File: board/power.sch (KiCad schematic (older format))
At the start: 144 parts, among them P47 CONN_2, P48 CONN_2, SW1 SWITCH_INV, U14 TPS53319, U15 GBU15005-G, U16 TPS54560, U3 TPS54625, U4 TPS54625, U5 TPS54625, U6 TPS51200

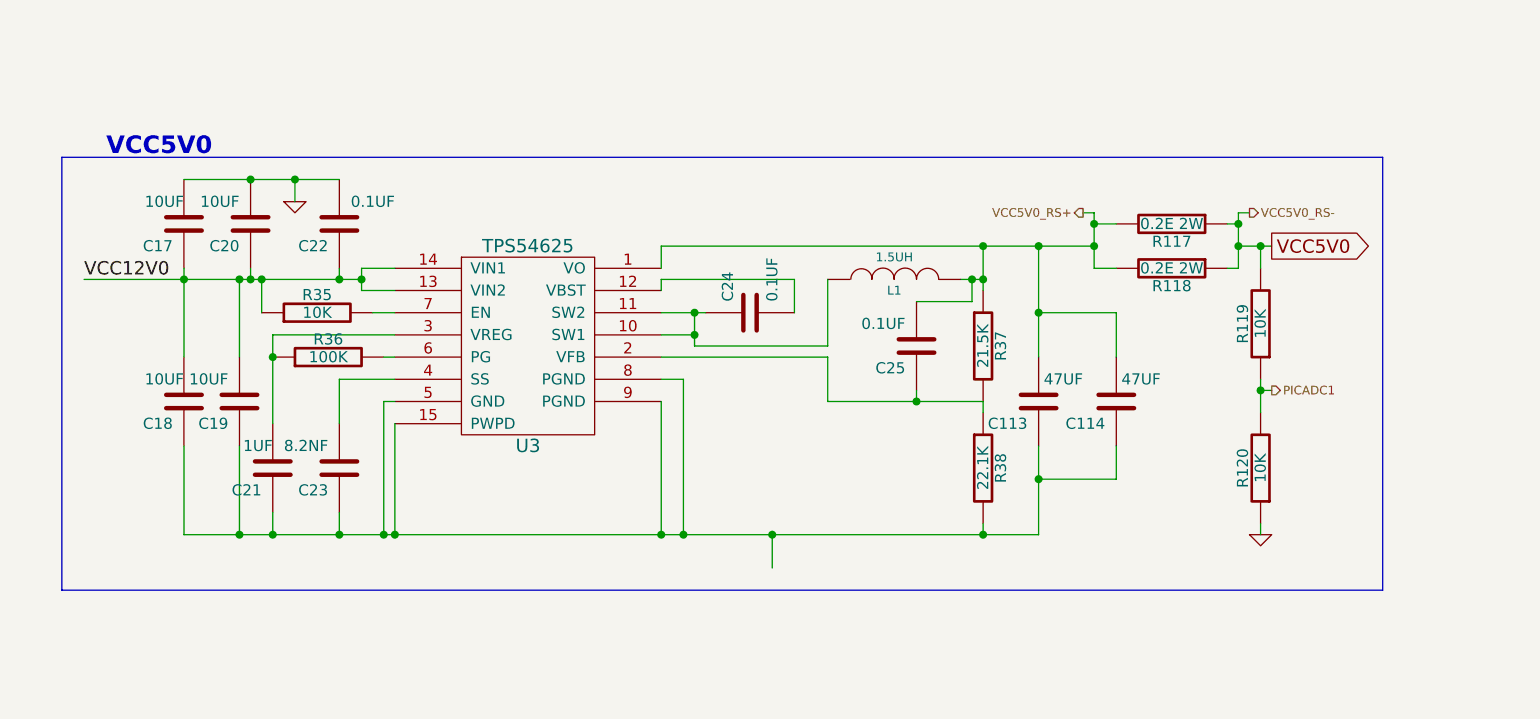
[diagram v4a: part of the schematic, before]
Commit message: Issue #934 - GTP routing
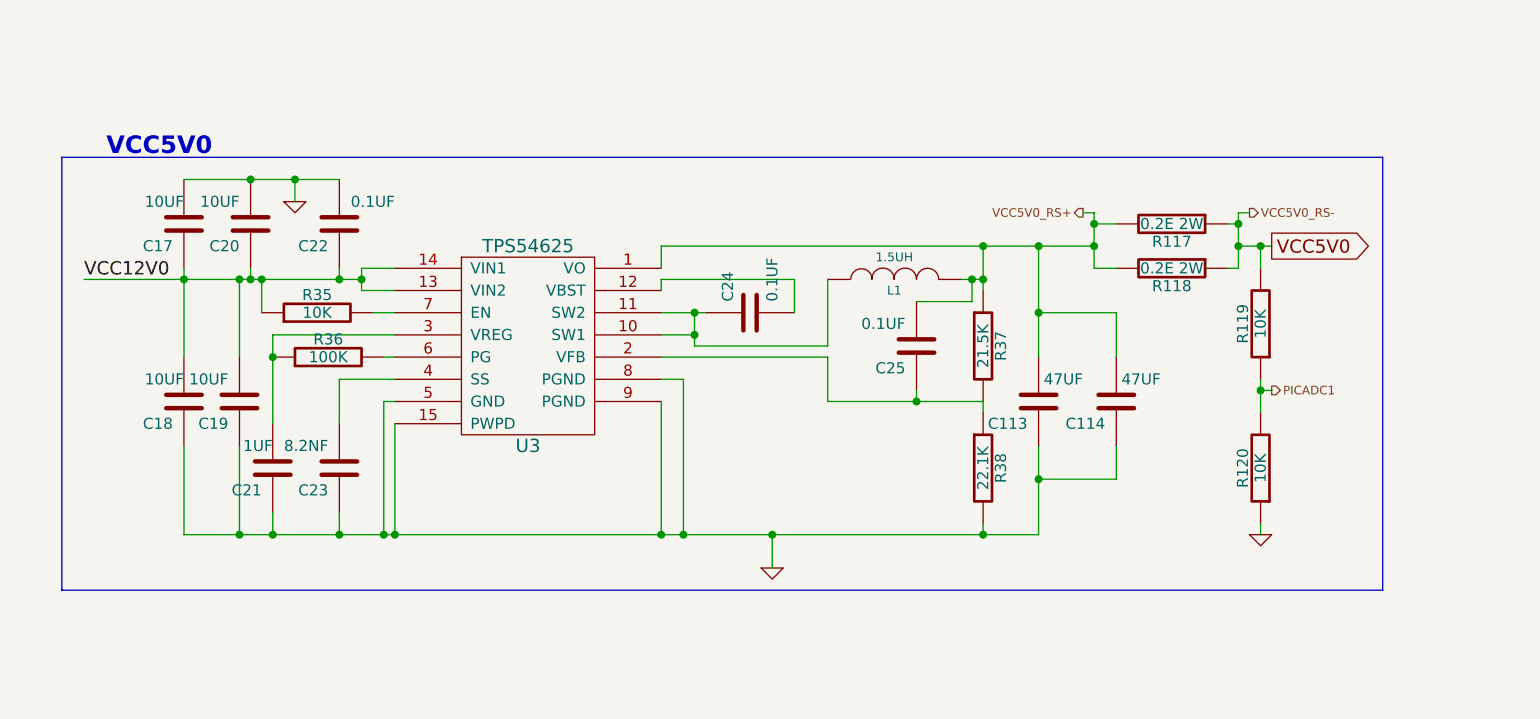
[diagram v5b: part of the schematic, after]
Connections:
- net GND: now also C113.1, C114.1, C18.1, C19.1, C21.1, C23.1, R38.2, U3.15 (PWPD), U3.5 (GND), U3.8 (PGND), U3.9 (PGND)
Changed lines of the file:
@@
 $Descr A3 16535 11693
 encoding utf-8
-Sheet 8 8
+Sheet 7 8
 Title "SP6N02"
-Date "27 feb 2014"
+Date "28 feb 2014"
 Rev "V1"
 Comp "Numato Lab"
@@
 $EndComp
 $Comp
-L GND #PWR12
+L GND #PWR03
 U 1 1 52DD9648
 P 11300 7700
-F 0 "#PWR12" H 11300 7700 30  0001 C CNN
+F 0 "#PWR03" H 11300 7700 30  0001 C CNN
 F 1 "GND" H 11300 7630 30  0001 C CNN
 F 2 "" H 11300 7700 60  0000 C CNN
@@
 $EndComp
 $Comp
-L GND #PWR16
+L GND #PWR04
 U 1 1 52DD9786
 P 12800 5350
-F 0 "#PWR16" H 12800 5350 30  0001 C CNN
+F 0 "#PWR04" H 12800 5350 30  0001 C CNN
 F 1 "GND" H 12800 5280 30  0001 C CNN
 F 2 "" H 12800 5350 60  0000 C CNN
@@
 $EndComp
 $Comp
-L GND #PWR15
+L GND #PWR05
 U 1 1 52DD9A04
 P 11500 1100
-F 0 "#PWR15" H 11500 1100 30  0001 C CNN
+F 0 "#PWR05" H 11500 1100 30  0001 C CNN
 F 1 "GND" H 11500 1030 30  0001 C CNN
 F 2 "" H 11500 1100 60  0000 C CNN
@@
 $EndComp
 $Comp
-L GND #PWR7
+L GND #PWR06
 U 1 1 52DD9A0A
 P 9400 2950
-F 0 "#PWR7" H 9400 2950 30  0001 C CNN
+F 0 "#PWR06" H 9400 2950 30  0001 C CNN
 F 1 "GND" H 9400 2880 30  0001 C CNN
 F 2 "" H 9400 2950 60  0000 C CNN
@@
 $EndComp
 $Comp
-L GND #PWR4
+L GND #PWR07
 U 1 1 52E1FEA6
 P 4000 1950
-F 0 "#PWR4" H 4000 1950 30  0001 C CNN
+F 0 "#PWR07" H 4000 1950 30  0001 C CNN
 F 1 "GND" H 4000 1880 30  0001 C CNN
 F 2 "" H 4000 1950 60  0000 C CNN
@@
 $EndComp
 $Comp
-L GND #PWR11
+L GND #PWR08
 U 1 1 52E4CA76
 P 10900 8600
-F 0 "#PWR11" H 10900 8600 30  0001 C CNN
+F 0 "#PWR08" H 10900 8600 30  0001 C CNN
 F 1 "GND" H 10900 8530 30  0001 C CNN
 F 2 "" H 10900 8600 60  0000 C CNN
@@
 $EndComp
 $Comp
-L GND #PWR8
+L GND #PWR09
 U 1 1 52E4CA88
 P 10450 9800
-F 0 "#PWR8" H 10450 9800 30  0001 C CNN
+F 0 "#PWR09" H 10450 9800 30  0001 C CNN
 F 1 "GND" H 10450 9730 30  0001 C CNN
 F 2 "" H 10450 9800 60  0000 C CNN
@@
 $EndComp
 $Comp
-L GND #PWR20
+L GND #PWR010
 U 1 1 52E4CAA0
 P 13800 9800
-F 0 "#PWR20" H 13800 9800 30  0001 C CNN
+F 0 "#PWR010" H 13800 9800 30  0001 C CNN
 F 1 "GND" H 13800 9730 30  0001 C CNN
 F 2 "" H 13800 9800 60  0000 C CNN
@@
 $EndComp
 $Comp
-L GND #PWR19
+L GND #PWR011
 U 1 1 52E4CAAC
 P 13200 9300
-F 0 "#PWR19" H 13200 9300 30  0001 C CNN
+F 0 "#PWR011" H 13200 9300 30  0001 C CNN
 F 1 "GND" H 13200 9230 30  0001 C CNN
 F 2 "" H 13200 9300 60  0000 C CNN
@@
 $EndComp
 $Comp
-L GND #PWR13
+L GND #PWR012
 U 1 1 52E4CAB8
 P 11350 9950
-F 0 "#PWR13" H 11350 9950 30  0001 C CNN
+F 0 "#PWR012" H 11350 9950 30  0001 C CNN
 F 1 "GND" H 11350 9880 30  0001 C CNN
 F 2 "" H 11350 9950 60  0000 C CNN
@@
 VCC3V3
 $Comp
-L GND #PWR17
+L GND #PWR013
 U 1 1 52E4CABF
 P 12800 9700
-F 0 "#PWR17" H 12800 9700 30  0001 C CNN
+F 0 "#PWR013" H 12800 9700 30  0001 C CNN
 F 1 "GND" H 12800 9630 30  0001 C CNN
 F 2 "" H 12800 9700 60  0000 C CNN
@@
 $EndComp
 $Comp
-L GND #PWR18
+L GND #PWR014
 U 1 1 52E4CACB
 P 13100 9950
-F 0 "#PWR18" H 13100 9950 30  0001 C CNN
+F 0 "#PWR014" H 13100 9950 30  0001 C CNN
 F 1 "GND" H 13100 9880 30  0001 C CNN
 F 2 "" H 13100 9950 60  0000 C CNN
@@
 $EndComp
 $Comp
-L GND #PWR9
+L GND #PWR015
 U 1 1 52F26CB0
 P 10650 3700
-F 0 "#PWR9" H 10650 3700 30  0001 C CNN
+F 0 "#PWR015" H 10650 3700 30  0001 C CNN
 F 1 "GND" H 10650 3630 30  0001 C CNN
 F 2 "" H 10650 3700 60  0000 C CNN
@@
 $EndComp
 $Comp
-L GND #PWR10
+L GND #PWR016
 U 1 1 52F2BB58
 P 10900 6200
-F 0 "#PWR10" H 10900 6200 30  0001 C CNN
+F 0 "#PWR016" H 10900 6200 30  0001 C CNN
 F 1 "GND" H 10900 6130 30  0001 C CNN
 F 2 "" H 10900 6200 60  0000 C CNN
@@
 $EndComp
 $Comp
-L GND #PWR14
+L GND #PWR017
 U 1 1 52F2C00C
 P 11450 6150
-F 0 "#PWR14" H 11450 6150 30  0001 C CNN
+F 0 "#PWR017" H 11450 6150 30  0001 C CNN
 F 1 "GND" H 11450 6080 30  0001 C CNN
 F 2 "" H 11450 6150 60  0000 C CNN
@@
 $EndComp
 $Comp
-L GND #PWR5
+L GND #PWR018
 U 1 1 52FA3E62
 P 6250 9400
-F 0 "#PWR5" H 6250 9400 30  0001 C CNN
+F 0 "#PWR018" H 6250 9400 30  0001 C CNN
 F 1 "GND" H 6250 9330 30  0001 C CNN
 F 2 "" H 6250 9400 60  0000 C CNN
@@
 $EndComp
 $Comp
-L GND #PWR3
+L GND #PWR019
 U 1 1 52FA3EB9
 P 1900 7900
-F 0 "#PWR3" H 1900 7900 30  0001 C CNN
+F 0 "#PWR019" H 1900 7900 30  0001 C CNN
 F 1 "GND" H 1900 7830 30  0001 C CNN
 F 2 "" H 1900 7900 60  0000 C CNN
@@
 	850  7700 6800 7700
 Wire Bus Line
-	6800 9650 6800 7700
+	6800 7700 6800 9650
 Wire Bus Line
-	850  9650 6800 9650
+	6800 9650 850  9650
 Connection ~ 4150 1250
 Wire Wire Line
@@
 	15100 9400 15100 9500
 $Comp
-L GND #PWR22
+L GND #PWR020
 U 1 1 530E4356
 P 15100 10050
-F 0 "#PWR22" H 15100 10050 30  0001 C CNN
+F 0 "#PWR020" H 15100 10050 30  0001 C CNN
 F 1 "GND" H 15100 9980 30  0001 C CNN
 F 2 "" H 15100 10050 60  0000 C CNN
@@
 	15250 6950 15250 7050
 $Comp
-L GND #PWR23
+L GND #PWR021
 U 1 1 530E4D62
 P 15250 7650
-F 0 "#PWR23" H 15250 7650 30  0001 C CNN
+F 0 "#PWR021" H 15250 7650 30  0001 C CNN
 F 1 "GND" H 15250 7580 30  0001 C CNN
 F 2 "" H 15250 7650 60  0000 C CNN
@@
 	15000 4750 15000 4850
 $Comp
-L GND #PWR21
+L GND #PWR022
 U 1 1 530E5A14
 P 15000 5400
-F 0 "#PWR21" H 15000 5400 30  0001 C CNN
+F 0 "#PWR022" H 15000 5400 30  0001 C CNN
 F 1 "GND" H 15000 5330 30  0001 C CNN
 F 2 "" H 15000 5400 60  0000 C CNN
@@
 	15300 2500 15300 2600
 $Comp
-L GND #PWR24
+L GND #PWR023
 U 1 1 530E6979
 P 15300 3150
-F 0 "#PWR24" H 15300 3150 30  0001 C CNN
+F 0 "#PWR023" H 15300 3150 30  0001 C CNN
 F 1 "GND" H 15300 3080 30  0001 C CNN
 F 2 "" H 15300 3150 60  0000 C CNN
@@
 	8050 2450 8050 2550
 $Comp
-L GND #PWR6
+L GND #PWR024
 U 1 1 530E7C33
 P 8050 3100
-F 0 "#PWR6" H 8050 3100 30  0001 C CNN
+F 0 "#PWR024" H 8050 3100 30  0001 C CNN
 F 1 "GND" H 8050 3030 30  0001 C CNN
 F 2 "" H 8050 3100 60  0000 C CNN
@@
 	8600 900  5550 900
 Wire Bus Line
-	850  7700 850  9650
+	850  9650 850  7700
+$Comp
+L GND #PWR?
+U 1 1 53108904
+P 4050 9550
+F 0 "#PWR?" H 4050 9550 30  0001 C CNN
+F 1 "GND" H 4050 9480 30  0001 C CNN
+F 2 "" H 4050 9550 60  0000 C CNN
+F 3 "" H 4050 9550 60  0000 C CNN
+	1    4050 9550
+	1    0    0    -1
+$EndComp
 $EndSCHEMATC

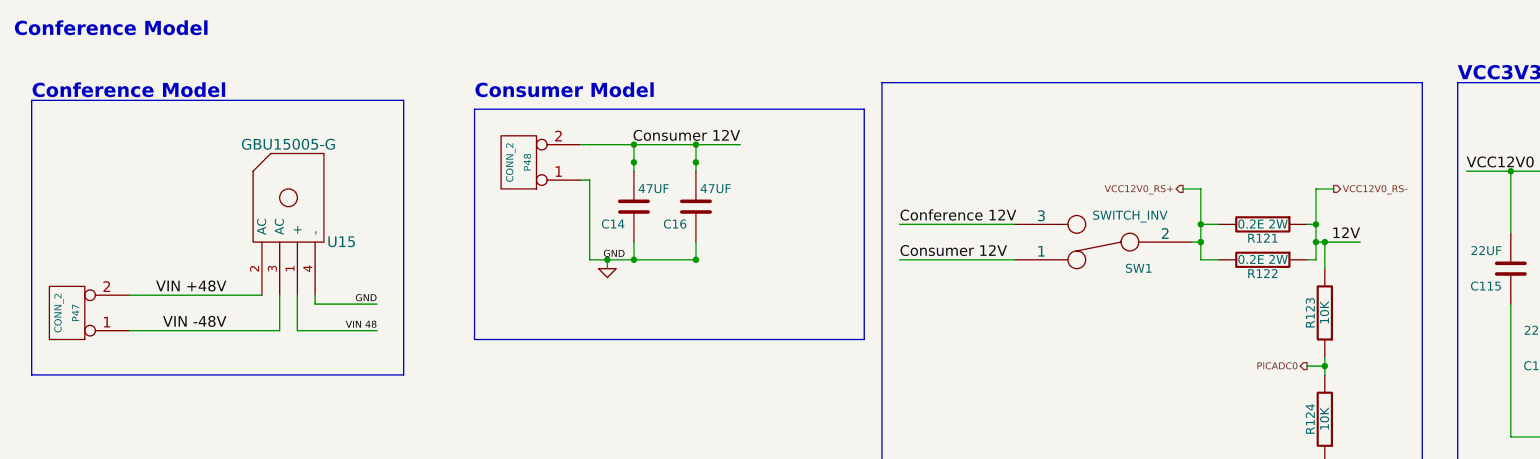
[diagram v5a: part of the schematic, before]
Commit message: Issue #1022 - Power supply
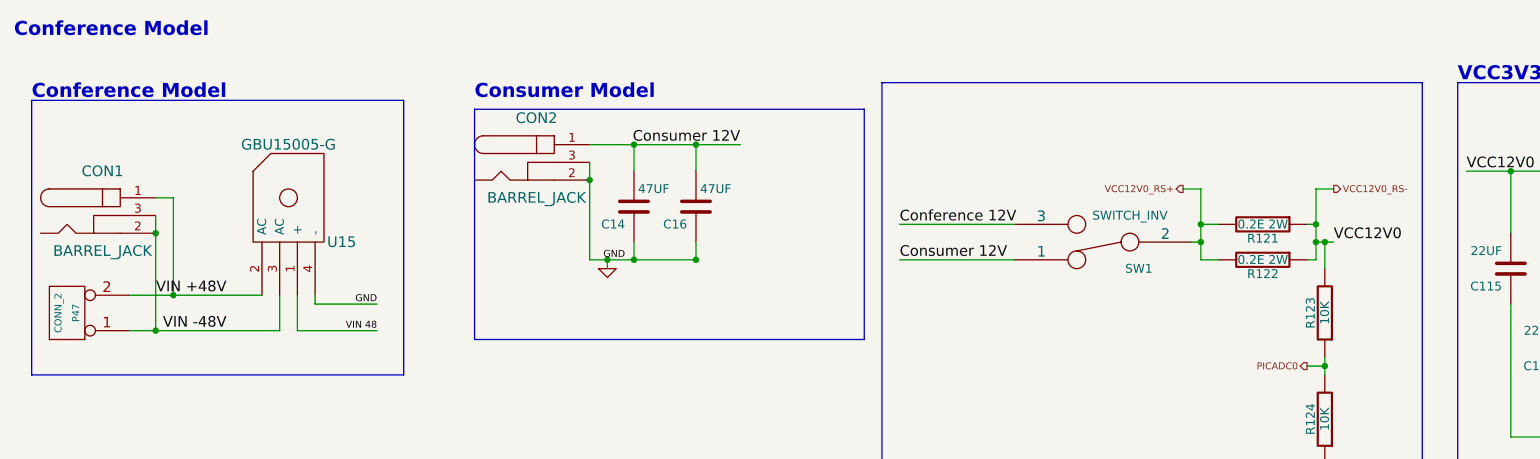
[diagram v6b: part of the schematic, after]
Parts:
- removed P48: CONN_2, symbol CONN_2
- added CON1, CON2: BARREL_JACK, symbol BARREL_JACK
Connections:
- net VCC12V0 is gone; now on net VCC12V0_RS-: C115.2, C116.1, C117.2, C119.1, C120.2, C121.2, C122.1, C125.2, C128.2, C129.2, C130.2, C131.1, C134.2, C135.2, C137.2, C17.1, C18.2, C19.2, C20.1, C22.1, R267.1, R35.1, R39.1, R42.1, U14.12 (VIN), U14.13 (VIN), U14.14 (VIN), U14.15 (VIN), U14.16 (VIN), U14.17 (VIN), U14.19 (VDD), U3.13 (VIN2), U3.14 (VIN1), U4.13 (VIN2), U4.14 (VIN1), U5.13 (VIN2), U5.14 (VIN1)
- net Consumer 12V: now also CON2.1
- net GND: now also CON2.2, CON2.3
- net VIN +48V: now also CON1.1
- net VIN -48V: now also CON1.2, CON1.3

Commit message: Issue #1022 - Power supply & pic& SCHEMATIC SECTION.
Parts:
- removed SW1: SWITCH_INV, ~, symbol SWITCH_INV
- added D28, D29, D30, D31: DIODESCH, ~, symbol DIODESCH
- added F1: FUSE, ~, symbol FUSE
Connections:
- net Conference 12V: now also D28.1 (A), D29.1 (A)
- net Consumer 12V: now also D30.1 (A), D31.1 (A)
- net DDR1V8: no longer C145.2, C150.2, C153.2, L2.2, R125.2, R126.2, R275.1, U4.1 (VO)
- net VCC12V0_RS+: now also F1.2
- new net: D28.2 (K), D29.2 (K), D30.2 (K), D31.2 (K), F1.1
- new net DDR1V8_RS+: C145.2, C150.2, C153.2, L2.2, R125.2, R126.2, R275.1, U4.1 (VO)
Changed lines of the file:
@@
 $Descr A3 16535 11693
 encoding utf-8
-Sheet 7 8
+Sheet 6 8
 Title "SP6N02"
-Date "14 mar 2014"
+Date "18 mar 2014"
 Rev "V1"
 Comp "Numato Lab"
@@
 	-1   0    0    1
 $EndComp
-Text Label 13500 3900 0    60   ~ 0
-DDR1V8
 Text GLabel 15550 1850 2    60   Output ~ 0
 VCC3V3
@@
 	1    0    0    -1
 $EndComp
-$Comp
-L SWITCH_INV SW1
-U 1 1 53060B27
-P 6800 1800
-F 0 "SW1" H 6600 1950 50  0000 C CNN
-F 1 "SWITCH_INV" H 6650 1650 50  0000 C CNN
-F 2 "~" H 6800 1800 60  0000 C CNN
-F 3 "~" H 6800 1800 60  0000 C CNN
-	1    6800 1800
-	-1   0    0    1
-$EndComp
 Text Label 8100 1800 0    60   ~ 0
 VCC12V0
-Text Label 5650 1900 0    60   ~ 0
+Text Label 5600 2000 0    60   ~ 0
 Consumer 12V
 Text Label 1850 2300 2    60   ~ 0
@@
 Text Label 2700 2150 2    39   ~ 0
 GND
-Text Label 5650 1700 0    60   ~ 0
+Text Label 5550 1350 0    60   ~ 0
 Conference 12V
 Text Label 4750 1250 2    60   ~ 0
@@
 	2350 2150 2700 2150
 Wire Wire Line
-	5650 1700 6300 1700
+	5550 1350 6200 1350
 Wire Wire Line
-	5650 1900 6300 1900
+	5600 2000 6250 2000
 Wire Wire Line
 	2150 2300 2150 2100
@@
 Wire Wire Line
 	15300 3100 15300 3150
-Wire Wire Line
-	7300 1800 7350 1800
 Connection ~ 7350 1800
 Connection ~ 8000 1800
@@
 Wire Wire Line
 	8000 1800 8100 1800
+$Comp
+L DIODESCH D28
+U 1 1 532F293D
+P 6400 1350
+F 0 "D28" H 6400 1450 40  0000 C CNN
+F 1 "DIODESCH" H 6400 1550 40  0000 C CNN
+F 2 "~" H 6400 1350 60  0000 C CNN
+F 3 "~" H 6400 1350 60  0000 C CNN
+	1    6400 1350
+	1    0    0    -1
+$EndComp
+$Comp
+L DIODESCH D31
+U 1 1 532F294A
+P 6450 2300
+F 0 "D31" H 6450 2400 40  0000 C CNN
+F 1 "DIODESCH" H 6450 2200 40  0000 C CNN
+F 2 "~" H 6450 2300 60  0000 C CNN
+F 3 "~" H 6450 2300 60  0000 C CNN
+	1    6450 2300
+	1    0    0    -1
+$EndComp
+$Comp
+L DIODESCH D30
+U 1 1 532F2950
+P 6450 2000
+F 0 "D30" H 6450 2100 40  0000 C CNN
+F 1 "DIODESCH" H 6450 1900 40  0000 C CNN
+F 2 "~" H 6450 2000 60  0000 C CNN
+F 3 "~" H 6450 2000 60  0000 C CNN
+	1    6450 2000
+	1    0    0    -1
+$EndComp
+$Comp
+L DIODESCH D29
+U 1 1 532F2956
+P 6400 1550
+F 0 "D29" H 6400 1650 40  0000 C CNN
+F 1 "DIODESCH" H 6400 1450 40  0000 C CNN
+F 2 "~" H 6400 1550 60  0000 C CNN
+F 3 "~" H 6400 1550 60  0000 C CNN
+	1    6400 1550
+	1    0    0    -1
+$EndComp
+Wire Wire Line
+	6200 1350 6200 1550
+Wire Wire Line
+	6600 1350 6600 1550
+Wire Wire Line
+	6250 2000 6250 2300
+Wire Wire Line
+	6650 2300 6650 2000
+Wire Wire Line
+	6650 2150 6750 2150
+Wire Wire Line
+	6750 2150 6750 1450
+Wire Wire Line
+	6750 1450 6600 1450
+Connection ~ 6600 1450
+Connection ~ 6650 2150
+$Comp
+L FUSE F1
+U 1 1 532F3994
+P 7050 1800
+F 0 "F1" H 7150 1850 40  0000 C CNN
+F 1 "FUSE" H 6950 1750 40  0000 C CNN
+F 2 "~" H 7050 1800 60  0000 C CNN
+F 3 "~" H 7050 1800 60  0000 C CNN
+	1    7050 1800
+	1    0    0    -1
+$EndComp
+Wire Wire Line
+	6800 1800 6750 1800
+Connection ~ 6750 1800
+Wire Wire Line
+	7300 1800 7350 1800
 $EndSCHEMATC
